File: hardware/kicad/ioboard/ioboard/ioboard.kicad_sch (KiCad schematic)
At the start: 0 parts

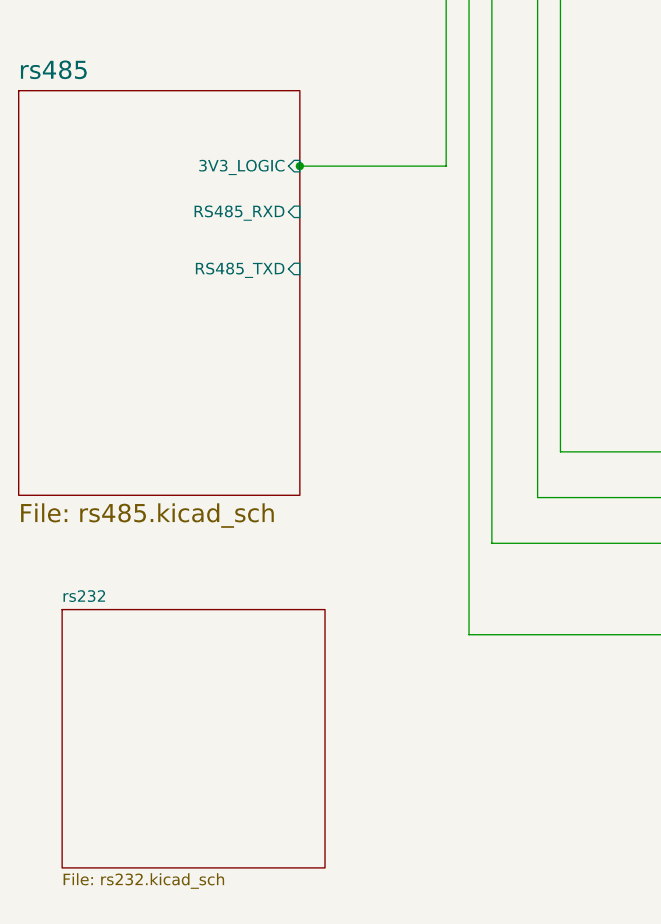
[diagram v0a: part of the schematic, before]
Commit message: Add RS232 schematic capture and wire it into the root sheet
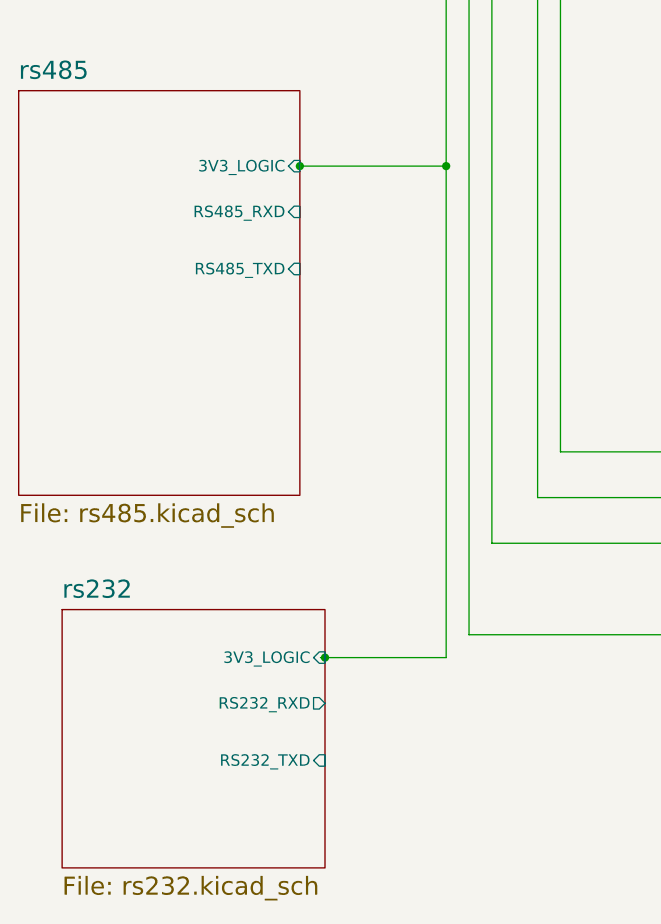
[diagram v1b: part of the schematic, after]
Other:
- sheet rs232 ports: added 3V3_LOGIC, RS232_RXD, RS232_TXD; removed none
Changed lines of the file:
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@@
 	(paper "A4")
+	(junction
+		(at 65.278 167.64)
+		(diameter 0)
+		(color 0 0 0 0)
+	)
 	(junction
 		(at 78.74 38.1)
@@
 	)
 	(junction
+		(at 78.74 113.03)
+		(diameter 0)
+		(color 0 0 0 0)
+	)
+	(junction
 		(at 83.82 38.1)
 		(diameter 0)
@@
 	(wire
 		(pts
+			(xy 78.74 167.64) (xy 78.74 113.03)
+		)
+		(stroke
+			(width 0)
+			(type default)
+		)
+	)
+	(wire
+		(pts
 			(xy 102.87 88.9) (xy 93.98 88.9)
 		)
@@
 	(wire
 		(pts
+			(xy 64.77 167.64) (xy 65.278 167.64)
+		)
+		(stroke
+			(width 0)
+			(type default)
+		)
+	)
+	(wire
+		(pts
 			(xy 88.9 149.86) (xy 107.95 149.86)
 		)
@@
 		(pts
 			(xy 91.44 58.42) (xy 91.44 144.78)
+		)
+		(stroke
+			(width 0)
+			(type default)
+		)
+	)
+	(wire
+		(pts
+			(xy 65.278 167.64) (xy 78.74 167.64)
 		)
 		(stroke
@@
 		)
 		(property "Sheetname" "rs232"
-			(at 36.068 161.5944 0)
-			(effects
-				(font
-					(size 1.27 1.27)
+			(at 36.068 161.2294 0)
+			(effects
+				(font
+					(size 2 2)
 				)
 				(justify left bottom)
@@
 		)
 		(property "Sheetfile" "rs232.kicad_sch"
-			(at 36.068 191.5926 0)
-			(effects
-				(font
-					(size 1.27 1.27)
+			(at 36.068 191.8846 0)
+			(effects
+				(font
+					(size 2 2)
 				)
 				(justify left top)
 			)
 		)
+		(pin "3V3_LOGIC" input
+			(at 65.278 167.64 0)
+			(effects
+				(font
+					(size 1.27 1.27)
+				)
+				(justify right)
+			)
+		)
+		(pin "RS232_RXD" output
+			(at 65.278 172.72 0)
+			(effects
+				(font
+					(size 1.27 1.27)
+				)
+				(justify right)
+			)
+		)
+		(pin "RS232_TXD" input
+			(at 65.278 179.07 0)
+			(effects
+				(font
+					(size 1.27 1.27)
+				)
+				(justify right)
+			)
+		)
